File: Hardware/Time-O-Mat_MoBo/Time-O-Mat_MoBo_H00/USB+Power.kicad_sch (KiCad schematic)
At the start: 23 parts, among them J7 TYPE-C-31-M-12, Q2 S8050, Q3 S8050, U4 AMS1117-3.3, U5 CH340G, Y2 12MHz

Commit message: Created segment PCB
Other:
- note added: "Nebo asi stejný footprint 918-418K2023S40001"
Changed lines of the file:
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@@
     (stroke (width 0) (type default) (color 0 0 0 0))
+  )
+  (text "Nebo asi stejný footprint\n918-418K2023S40001" (at 54.61 110.49 0)
+    (effects (font (size 1.27 1.27)) (justify left bottom))
   )
   (label "D+" (at 87.63 76.2 0)

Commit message: HW update
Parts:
- removed C15, C17: 22p, Capacitor_SMD:C_0603_1608Metric, symbol Device:C
- removed Y2: 12MHz, Crystal:Crystal_HC49-4H_Vertical, symbol Device:Crystal
- U5: symbol Interface_USB:CH340G -> Interface_USB:CH340C; LCSC C14267 -> C84681
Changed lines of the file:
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@@
 (kicad_sch (version 20211123) (generator eeschema)
   (paper "A4")
-  (junction (at 127 86.36) (diameter 0) (color 0 0 0 0)
-  )
   (junction (at 113.03 128.27) (diameter 0) (color 0 0 0 0)
   )
@@
   )
   (junction (at 140.97 128.27) (diameter 0) (color 0 0 0 0)
-  )
-  (junction (at 116.84 86.36) (diameter 0) (color 0 0 0 0)
   )
   (junction (at 121.92 68.58) (diameter 0) (color 0 0 0 0)
@@
     (stroke (width 0) (type default) (color 0 0 0 0))
   )
-  (wire (pts (xy 118.11 86.36) (xy 116.84 86.36))
-    (stroke (width 0) (type default) (color 0 0 0 0))
-  )
   (wire (pts (xy 113.03 73.66) (xy 78.74 73.66))
     (stroke (width 0) (type default) (color 0 0 0 0))
@@
     (stroke (width 0) (type default) (color 0 0 0 0))
   )
-  (wire (pts (xy 127 87.63) (xy 127 86.36))
-    (stroke (width 0) (type default) (color 0 0 0 0))
-  )
   (wire (pts (xy 78.74 64.77) (xy 78.74 63.5))
     (stroke (width 0) (type default) (color 0 0 0 0))
@@
     (stroke (width 0) (type default) (color 0 0 0 0))
   )
-  (wire (pts (xy 127 86.36) (xy 129.54 86.36))
-    (stroke (width 0) (type default) (color 0 0 0 0))
-  )
   (wire (pts (xy 115.57 73.66) (xy 129.54 73.66))
     (stroke (width 0) (type default) (color 0 0 0 0))
   )
-  (wire (pts (xy 116.84 81.28) (xy 116.84 86.36))
-    (stroke (width 0) (type default) (color 0 0 0 0))
-  )
   (wire (pts (xy 162.56 73.66) (xy 166.37 73.66))
     (stroke (width 0) (type default) (color 0 0 0 0))
@@
     (stroke (width 0) (type default) (color 0 0 0 0))
   )
-  (wire (pts (xy 116.84 81.28) (xy 129.54 81.28))
-    (stroke (width 0) (type default) (color 0 0 0 0))
-  )
   (wire (pts (xy 129.54 76.2) (xy 115.57 76.2))
     (stroke (width 0) (type default) (color 0 0 0 0))
   )
-  (wire (pts (xy 116.84 87.63) (xy 116.84 86.36))
-    (stroke (width 0) (type default) (color 0 0 0 0))
-  )
   (wire (pts (xy 113.03 60.96) (xy 121.92 60.96))
     (stroke (width 0) (type default) (color 0 0 0 0))
@@
   )
   (wire (pts (xy 121.92 68.58) (xy 113.03 68.58))
-    (stroke (width 0) (type default) (color 0 0 0 0))
-  )
-  (wire (pts (xy 125.73 86.36) (xy 127 86.36))
     (stroke (width 0) (type default) (color 0 0 0 0))
   )
@@
     (pin "1")
   )
-  (symbol (lib_id "Device:C") (at 116.84 91.44 0) (unit 1)
-    (in_bom yes) (on_board yes)
-    (property "Reference" "C15" (id 0) (at 119.761 90.2716 0)
-      (effects (font (size 1.27 1.27)) (justify left))
-    )
-    (property "Value" "22p" (id 1) (at 119.761 92.583 0)
-      (effects (font (size 1.27 1.27)) (justify left))
-    )
-    (property "Footprint" "Capacitor_SMD:C_0603_1608Metric" (id 2) (at 117.8052 95.25 0)
-      (effects (font (size 1.27 1.27)) hide)
-    )
-    (property "Datasheet" "~" (id 3) (at 116.84 91.44 0)
-      (effects (font (size 1.27 1.27)) hide)
-    )
-    (property "LCSC" "C1653" (id 4) (at 116.84 91.44 0)
-      (effects (font (size 1.27 1.27)) hide)
-    )
-    (pin "1")
-    (pin "2")
-  )
   (symbol (lib_id "power:GND") (at 152.4 135.89 0) (unit 1)
     (in_bom yes) (on_board yes)
@@
     )
     (pin "1")
-  )
-  (symbol (lib_id "Device:C") (at 127 91.44 0) (unit 1)
-    (in_bom yes) (on_board yes)
-    (property "Reference" "C17" (id 0) (at 129.921 90.2716 0)
-      (effects (font (size 1.27 1.27)) (justify left))
-    )
-    (property "Value" "22p" (id 1) (at 129.921 92.583 0)
-      (effects (font (size 1.27 1.27)) (justify left))
-    )
-    (property "Footprint" "Capacitor_SMD:C_0603_1608Metric" (id 2) (at 127.9652 95.25 0)
-      (effects (font (size 1.27 1.27)) hide)
-    )
-    (property "Datasheet" "~" (id 3) (at 127 91.44 0)
-      (effects (font (size 1.27 1.27)) hide)
-    )
-    (property "LCSC" "C1653" (id 4) (at 127 91.44 0)
-      (effects (font (size 1.27 1.27)) hide)
-    )
-    (pin "1")
-    (pin "2")
   )
   (symbol (lib_id "Device:C") (at 102.87 132.08 0) (unit 1)
@@
     (pin "1")
     (pin "2")
-  )
-  (symbol (lib_id "power:GND") (at 127 95.25 0) (unit 1)
-    (in_bom yes) (on_board yes)
-    (property "Reference" "#PWR0149" (id 0) (at 127 101.6 0)
-      (effects (font (size 1.27 1.27)) hide)
-    )
-    (property "Value" "GND" (id 1) (at 127.127 99.6442 0))
-    (property "Footprint" "" (id 2) (at 127 95.25 0)
-      (effects (font (size 1.27 1.27)) hide)
-    )
-    (property "Datasheet" "" (id 3) (at 127 95.25 0)
-      (effects (font (size 1.27 1.27)) hide)
-    )
-    (pin "1")
   )
   (symbol (lib_id "power:GND") (at 128.27 135.89 0) (unit 1)
@@
     (pin "1")
   )
-  (symbol (lib_id "Interface_USB:CH340G") (at 139.7 76.2 0) (unit 1)
+  (symbol (lib_id "Interface_USB:CH340C") (at 139.7 76.2 0) (unit 1)
     (in_bom yes) (on_board yes)
     (property "Reference" "U5" (id 0) (at 143.51 90.17 0))
@@
       (effects (font (size 1.27 1.27)) (justify left) hide)
     )
-    (property "Datasheet" "http://www.datasheet5.com/pdf-local-2195953" (id 3) (at 130.81 55.88 0)
-      (effects (font (size 1.27 1.27)) hide)
-    )
-    (property "LCSC" "C14267" (id 4) (at 139.7 76.2 0)
+    (property "Datasheet" "https://datasheet.lcsc.com/szlcsc/Jiangsu-Qin-Heng-CH340C_C84681.pdf" (id 3) (at 130.81 55.88 0)
+      (effects (font (size 1.27 1.27)) hide)
+    )
+    (property "LCSC" "C84681" (id 4) (at 139.7 76.2 0)
       (effects (font (size 1.27 1.27)) hide)
     )
@@
     (pin "2")
   )
-  (symbol (lib_id "Device:Crystal") (at 121.92 86.36 0) (unit 1)
-    (in_bom yes) (on_board yes)
-    (property "Reference" "Y2" (id 0) (at 120.65 82.55 0))
-    (property "Value" "12MHz" (id 1) (at 127 83.82 0))
-    (property "Footprint" "Crystal:Crystal_HC49-4H_Vertical" (id 2) (at 121.92 86.36 0)
-      (effects (font (size 1.27 1.27)) hide)
-    )
-    (property "Datasheet" "~" (id 3) (at 121.92 86.36 0)
-      (effects (font (size 1.27 1.27)) hide)
-    )
-    (pin "1")
-    (pin "2")
-  )
   (symbol (lib_id "power:GND") (at 139.7 91.44 0) (unit 1)
     (in_bom yes) (on_board yes)
@@
     (pin "2")
   )
-  (symbol (lib_id "power:GND") (at 116.84 95.25 0) (unit 1)
-    (in_bom yes) (on_board yes)
-    (property "Reference" "#PWR0154" (id 0) (at 116.84 101.6 0)
-      (effects (font (size 1.27 1.27)) hide)
-    )
-    (property "Value" "GND" (id 1) (at 116.967 99.6442 0))
-    (property "Footprint" "" (id 2) (at 116.84 95.25 0)
-      (effects (font (size 1.27 1.27)) hide)
-    )
-    (property "Datasheet" "" (id 3) (at 116.84 95.25 0)
-      (effects (font (size 1.27 1.27)) hide)
-    )
-    (pin "1")
-  )
   (symbol (lib_id "Device:R") (at 83.82 60.96 0) (unit 1)

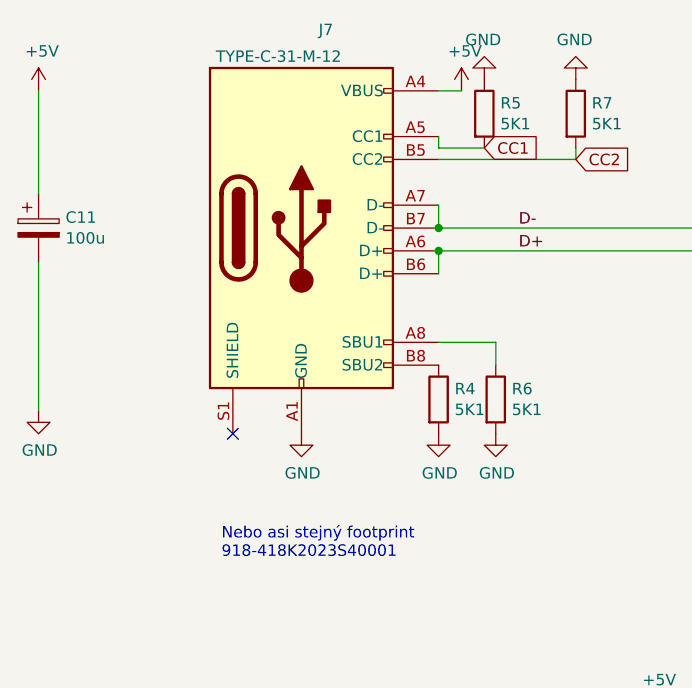
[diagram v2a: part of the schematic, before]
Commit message: Exported up to date STEP models and manufacturing data
Exported up to date 3D models of all PCB parts.
Created new subpanels fot manufacturing to counteract duplicit designators on different boards.
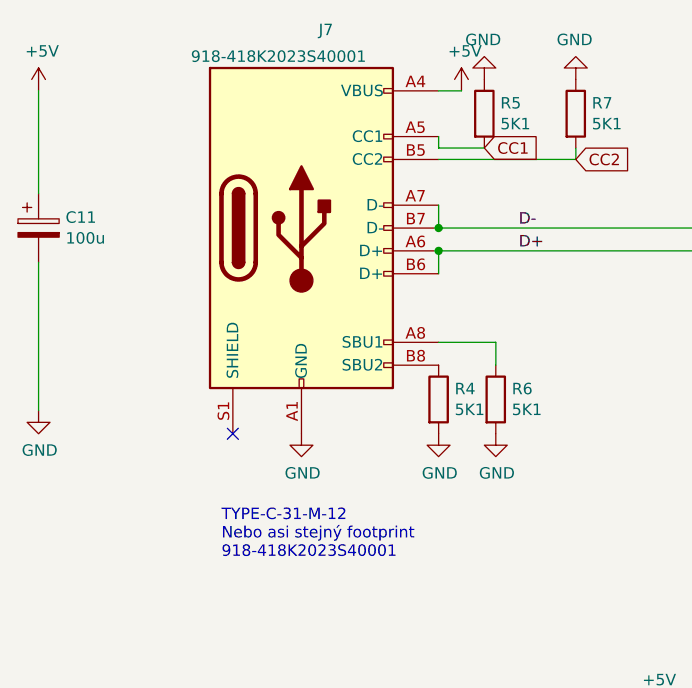
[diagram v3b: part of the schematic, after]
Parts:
- J7: value TYPE-C-31-M-12 -> 918-418K2023S40001; LCSC C165948 -> C167321
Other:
- note added: "TYPE-C-31-M-12 Nebo asi stejný footprint 918-418K2023S40001"
- note removed: "Nebo asi stejný footprint 918-418K2023S40001"
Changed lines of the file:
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@@
     (stroke (width 0) (type default) (color 0 0 0 0))
   )
-  (text "Nebo asi stejný footprint\n918-418K2023S40001" (at 54.61 110.49 0)
+  (text "TYPE-C-31-M-12\nNebo asi stejný footprint\n918-418K2023S40001"
+    (at 54.61 110.49 0)
     (effects (font (size 1.27 1.27)) (justify left bottom))
   )
@@
     (in_bom yes) (on_board yes)
     (property "Reference" "J7" (id 0) (at 66.2178 51.6382 0))
-    (property "Value" "TYPE-C-31-M-12" (id 1) (at 60.96 54.61 0))
+    (property "Value" "918-418K2023S40001" (id 1) (at 60.96 54.61 0))
     (property "Footprint" "Connector_USB:USB_C_Receptacle_HRO_TYPE-C-31-M-12" (id 2) (at 67.31 73.66 0)
       (effects (font (size 1.27 1.27)) hide)
@@
       (effects (font (size 1.27 1.27)) hide)
     )
-    (property "LCSC" "C165948" (id 4) (at 63.5 73.66 0)
+    (property "LCSC" "C167321" (id 4) (at 63.5 73.66 0)
       (effects (font (size 1.27 1.27)) hide)
     )
